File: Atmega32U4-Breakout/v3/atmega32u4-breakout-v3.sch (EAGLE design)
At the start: 58 parts, among them IC1 REG1117, U1 ATMEGA32U4

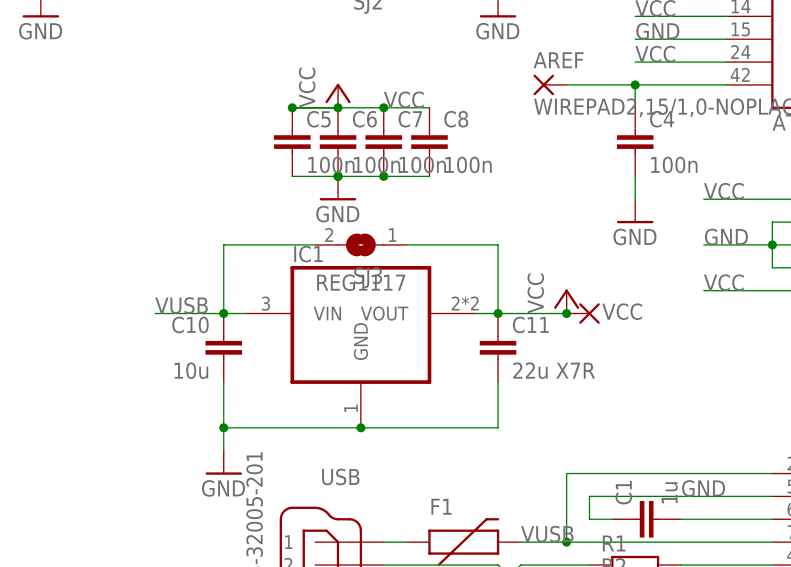
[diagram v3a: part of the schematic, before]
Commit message: Nudge some more stuff around, change silkscreen, add large GND pad on bottom, add multicb gerber job
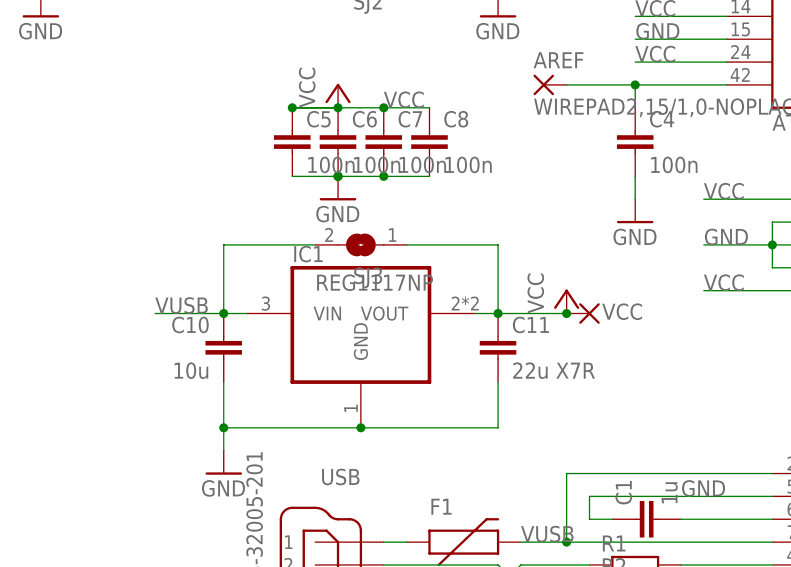
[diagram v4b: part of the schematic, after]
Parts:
- IC1: value REG1117 -> REG1117NP; device burr-brown:REG1117 -> burr-brown:REG1117NP
- SJ3: device jumper:SJ -> jumper:SJNP
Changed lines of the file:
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@@
 <part name="GND6" library="supply1" deviceset="GND" device=""/>
 <part name="P+5" library="supply1" deviceset="VCC" device=""/>
-<part name="IC1" library="burr-brown" deviceset="REG1117" device=""/>
-<part name="SJ3" library="jumper" deviceset="SJ" device=""/>
+<part name="IC1" library="burr-brown" deviceset="REG1117" device="NP" value="REG1117NP"/>
+<part name="SJ3" library="jumper" deviceset="SJ" device="NP"/>
 <part name="RESET1" library="jocki" deviceset="SMDSWITCH" device="EDRAGON1" value="SMDSWITCHEDRAGON1"/>
 <part name="BOOT1" library="jocki" deviceset="SMDSWITCH" device="EDRAGON1" value="SMDSWITCHEDRAGON1"/>

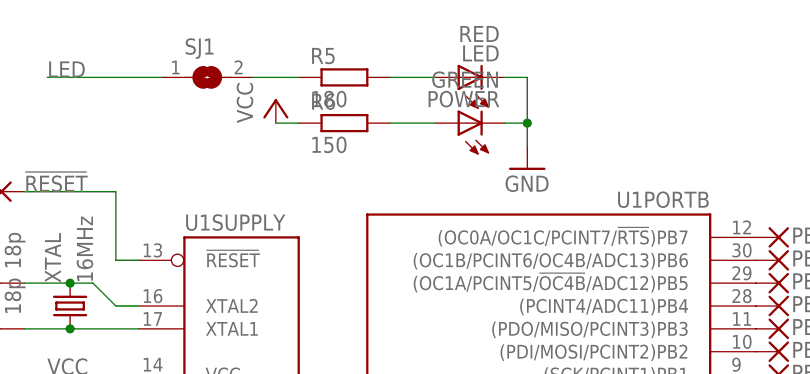
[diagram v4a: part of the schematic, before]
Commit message: Change red LED to blue, adapt dropper resistor
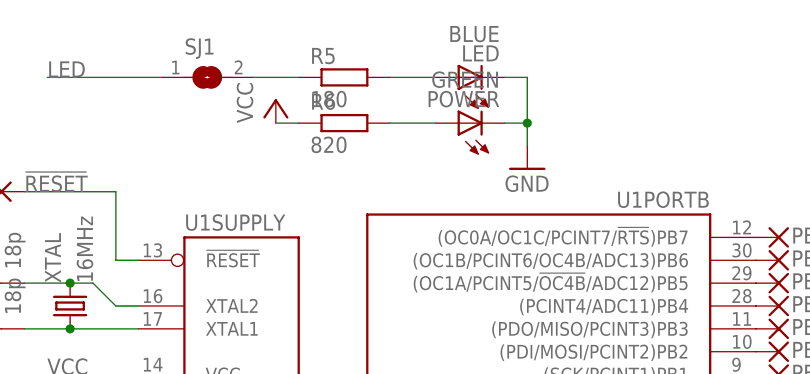
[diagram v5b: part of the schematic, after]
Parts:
- LED: value RED -> BLUE
- R6: value 150 -> 820
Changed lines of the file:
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@@
 <grid distance="0.1" unitdist="inch" unit="inch" style="lines" multiple="1" display="no" altdistance="0.01" altunitdist="inch" altunit="inch"/>
 <layers>
-<layer number="1" name="Top" color="4" fill="1" visible="yes" active="no"/>
-<layer number="16" name="Bottom" color="1" fill="1" visible="yes" active="no"/>
-<layer number="17" name="Pads" color="2" fill="1" visible="yes" active="no"/>
-<layer number="18" name="Vias" color="2" fill="1" visible="yes" active="no"/>
-<layer number="19" name="Unrouted" color="6" fill="1" visible="yes" active="no"/>
-<layer number="20" name="Dimension" color="15" fill="1" visible="yes" active="no"/>
-<layer number="21" name="tPlace" color="7" fill="1" visible="yes" active="no"/>
-<layer number="22" name="bPlace" color="7" fill="1" visible="yes" active="no"/>
-<layer number="23" name="tOrigins" color="15" fill="1" visible="yes" active="no"/>
-<layer number="24" name="bOrigins" color="15" fill="1" visible="yes" active="no"/>
-<layer number="25" name="tNames" color="7" fill="1" visible="yes" active="no"/>
-<layer number="26" name="bNames" color="7" fill="1" visible="yes" active="no"/>
-<layer number="27" name="tValues" color="7" fill="1" visible="yes" active="no"/>
-<layer number="28" name="bValues" color="7" fill="1" visible="yes" active="no"/>
+<layer number="1" name="Top" color="4" fill="1" visible="no" active="no"/>
+<layer number="16" name="Bottom" color="1" fill="1" visible="no" active="no"/>
+<layer number="17" name="Pads" color="2" fill="1" visible="no" active="no"/>
+<layer number="18" name="Vias" color="2" fill="1" visible="no" active="no"/>
+<layer number="19" name="Unrouted" color="6" fill="1" visible="no" active="no"/>
+<layer number="20" name="Dimension" color="15" fill="1" visible="no" active="no"/>
+<layer number="21" name="tPlace" color="7" fill="1" visible="no" active="no"/>
+<layer number="22" name="bPlace" color="7" fill="1" visible="no" active="no"/>
+<layer number="23" name="tOrigins" color="15" fill="1" visible="no" active="no"/>
+<layer number="24" name="bOrigins" color="15" fill="1" visible="no" active="no"/>
+<layer number="25" name="tNames" color="7" fill="1" visible="no" active="no"/>
+<layer number="26" name="bNames" color="7" fill="1" visible="no" active="no"/>
+<layer number="27" name="tValues" color="7" fill="1" visible="no" active="no"/>
+<layer number="28" name="bValues" color="7" fill="1" visible="no" active="no"/>
 <layer number="29" name="tStop" color="7" fill="3" visible="no" active="no"/>
 <layer number="30" name="bStop" color="7" fill="6" visible="no" active="no"/>
@@
 <layer number="35" name="tGlue" color="7" fill="4" visible="no" active="no"/>
 <layer number="36" name="bGlue" color="7" fill="5" visible="no" active="no"/>
-<layer number="37" name="tTest" color="7" fill="1" visible="yes" active="no"/>
-<layer number="38" name="bTest" color="7" fill="1" visible="yes" active="no"/>
+<layer number="37" name="tTest" color="7" fill="1" visible="no" active="no"/>
+<layer number="38" name="bTest" color="7" fill="1" visible="no" active="no"/>
 <layer number="39" name="tKeepout" color="4" fill="11" visible="no" active="no"/>
 <layer number="40" name="bKeepout" color="1" fill="11" visible="no" active="no"/>
@@
 <layer number="44" name="Drills" color="7" fill="1" visible="no" active="no"/>
 <layer number="45" name="Holes" color="7" fill="1" visible="no" active="no"/>
-<layer number="46" name="Milling" color="3" fill="1" visible="yes" active="no"/>
-<layer number="47" name="Measures" color="7" fill="1" visible="yes" active="no"/>
-<layer number="48" name="Document" color="7" fill="1" visible="yes" active="no"/>
-<layer number="49" name="Reference" color="7" fill="1" visible="yes" active="no"/>
-<layer number="50" name="dxf" color="7" fill="1" visible="yes" active="no"/>
-<layer number="51" name="tDocu" color="7" fill="1" visible="yes" active="no"/>
-<layer number="52" name="bDocu" color="7" fill="1" visible="yes" active="no"/>
-<layer number="53" name="tGND_GNDA" color="7" fill="9" visible="yes" active="no"/>
-<layer number="54" name="bGND_GNDA" color="1" fill="9" visible="yes" active="no"/>
-<layer number="56" name="wert" color="7" fill="1" visible="yes" active="no"/>
+<layer number="46" name="Milling" color="3" fill="1" visible="no" active="no"/>
+<layer number="47" name="Measures" color="7" fill="1" visible="no" active="no"/>
+<layer number="48" name="Document" color="7" fill="1" visible="no" active="no"/>
+<layer number="49" name="Reference" color="7" fill="1" visible="no" active="no"/>
+<layer number="50" name="dxf" color="7" fill="1" visible="no" active="no"/>
+<layer number="51" name="tDocu" color="7" fill="1" visible="no" active="no"/>
+<layer number="52" name="bDocu" color="7" fill="1" visible="no" active="no"/>
+<layer number="53" name="tGND_GNDA" color="7" fill="9" visible="no" active="no"/>
+<layer number="54" name="bGND_GNDA" color="1" fill="9" visible="no" active="no"/>
+<layer number="56" name="wert" color="7" fill="1" visible="no" active="no"/>
 <layer number="91" name="Nets" color="2" fill="1" visible="yes" active="yes"/>
 <layer number="92" name="Busses" color="1" fill="1" visible="yes" active="yes"/>
@@
 <part name="VCC" library="jocki" deviceset="WIREPAD" device="2,15/1,0-NOPLACE"/>
 <part name="R5" library="rcl" deviceset="R-EU_" device="R0603" value="180"/>
-<part name="R6" library="rcl" deviceset="R-EU_" device="R0603" value="150"/>
+<part name="R6" library="rcl" deviceset="R-EU_" device="R0603" value="820"/>
 <part name="SJ1" library="jumper" deviceset="SJ" device=""/>
-<part name="LED" library="led" deviceset="LED" device="CHIPLED_0805" value="RED"/>
+<part name="LED" library="led" deviceset="LED" device="CHIPLED_0805" value="BLUE"/>
 <part name="POWER" library="led" deviceset="LED" device="CHIPLED_0805" value="GREEN"/>
 <part name="GND8" library="supply1" deviceset="GND" device=""/>
